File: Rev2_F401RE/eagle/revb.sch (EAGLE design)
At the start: 162 parts, among them IC1 STM32F401RE, IC2 MCP73832, IC4 TPS63001, IC5 TPS63002, J1 USB4105-GF-A, J2 MEM2051-0019500A, J200 0, Q1 SI7615, T1 MMBTA06-7-F, T10 MMBTA06-7-F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

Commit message: Add barrel jack, add headers, add jumper between buck and rail, fix OLED pinout
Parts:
- added 3V3_EN, 5V_EN, 5V_OUT: (no value), pinhead:PINHD-1X2
- added CN1: (no value), adafruit:DCBARRELPTH
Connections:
- new net 3V3_BUCK: 3V3_EN.2, C208.1, C209.1, C210.1, C211.1, IC4.FB, IC4.VOUT
- new net 5V_BUCK: 5V_EN.2, C215.1, C216.1, C217.1, C218.1, IC5.FB, IC5.VOUT
- net +3V3: now also 3V3_EN.1; no longer C208.1, C209.1, C210.1, C211.1, IC4.FB, IC4.VOUT
- net +5V: now also 5V_EN.1, 5V_OUT.1; no longer C215.1, C216.1, C217.1, C218.1, IC5.FB, IC5.VOUT
- net GND: now also 5V_OUT.2, CN1.GND
- net USB_VIN: now also CN1.PWR
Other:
- note added: "Same footprint as 47352-1001"
- moved on the sheet: 3V3, 5V, D1, D100, J1, MIDI, R100, R101, R102, R103, R104, R105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

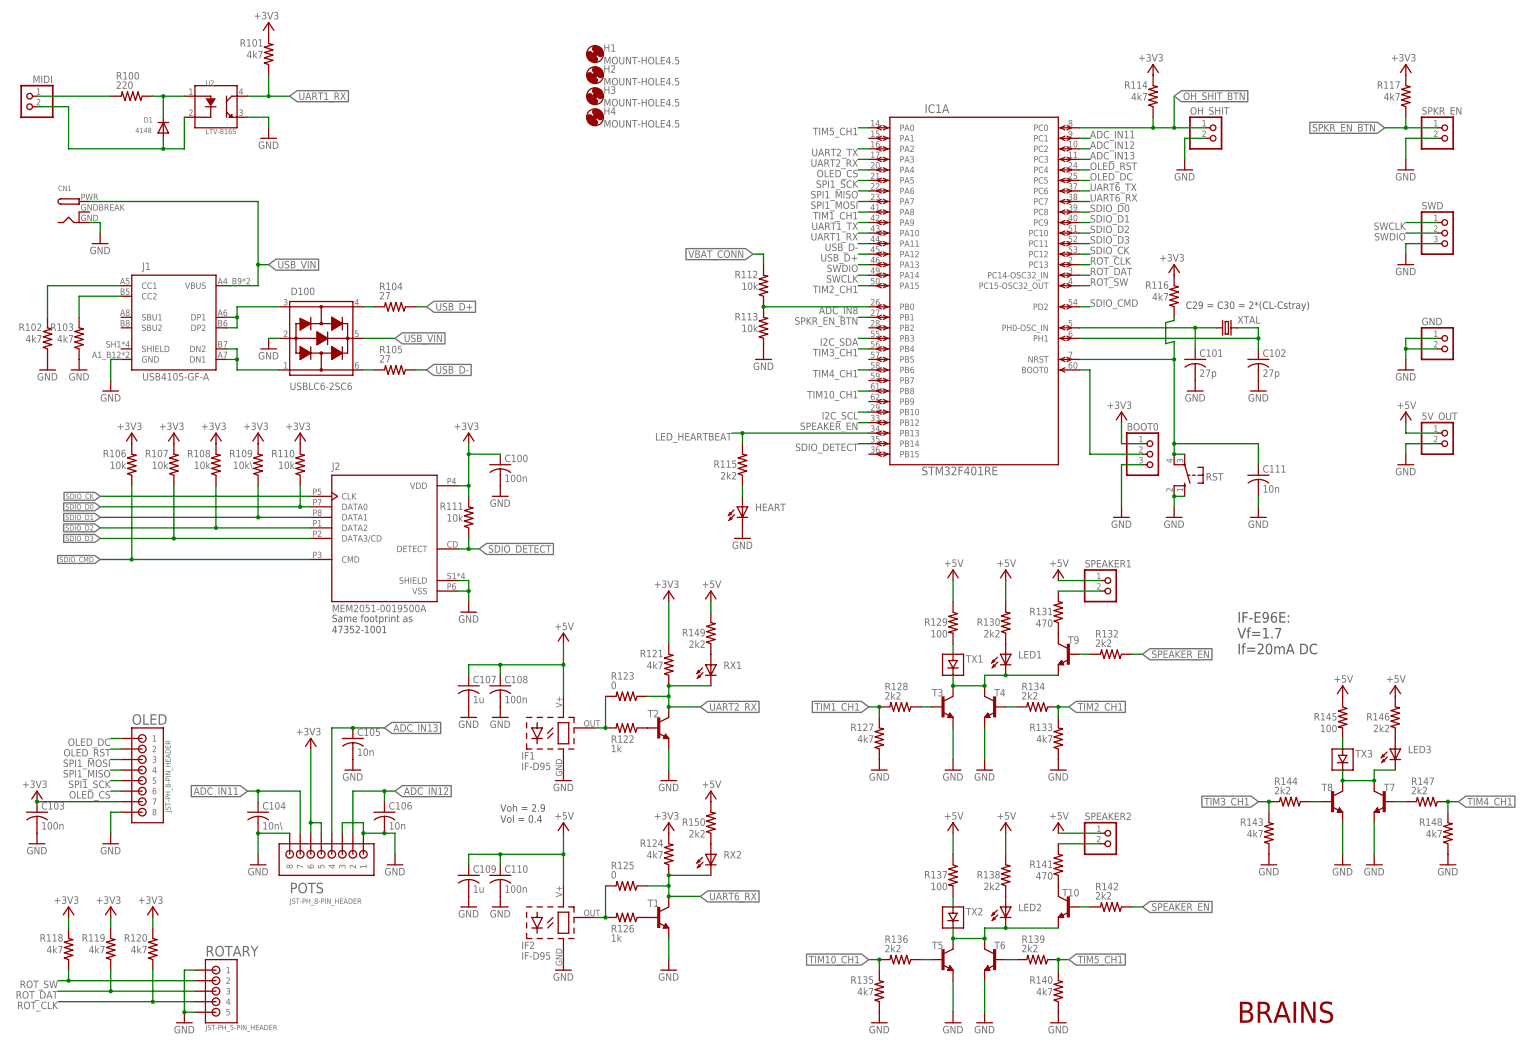
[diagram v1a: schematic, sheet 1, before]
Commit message: Add IO for a relay board
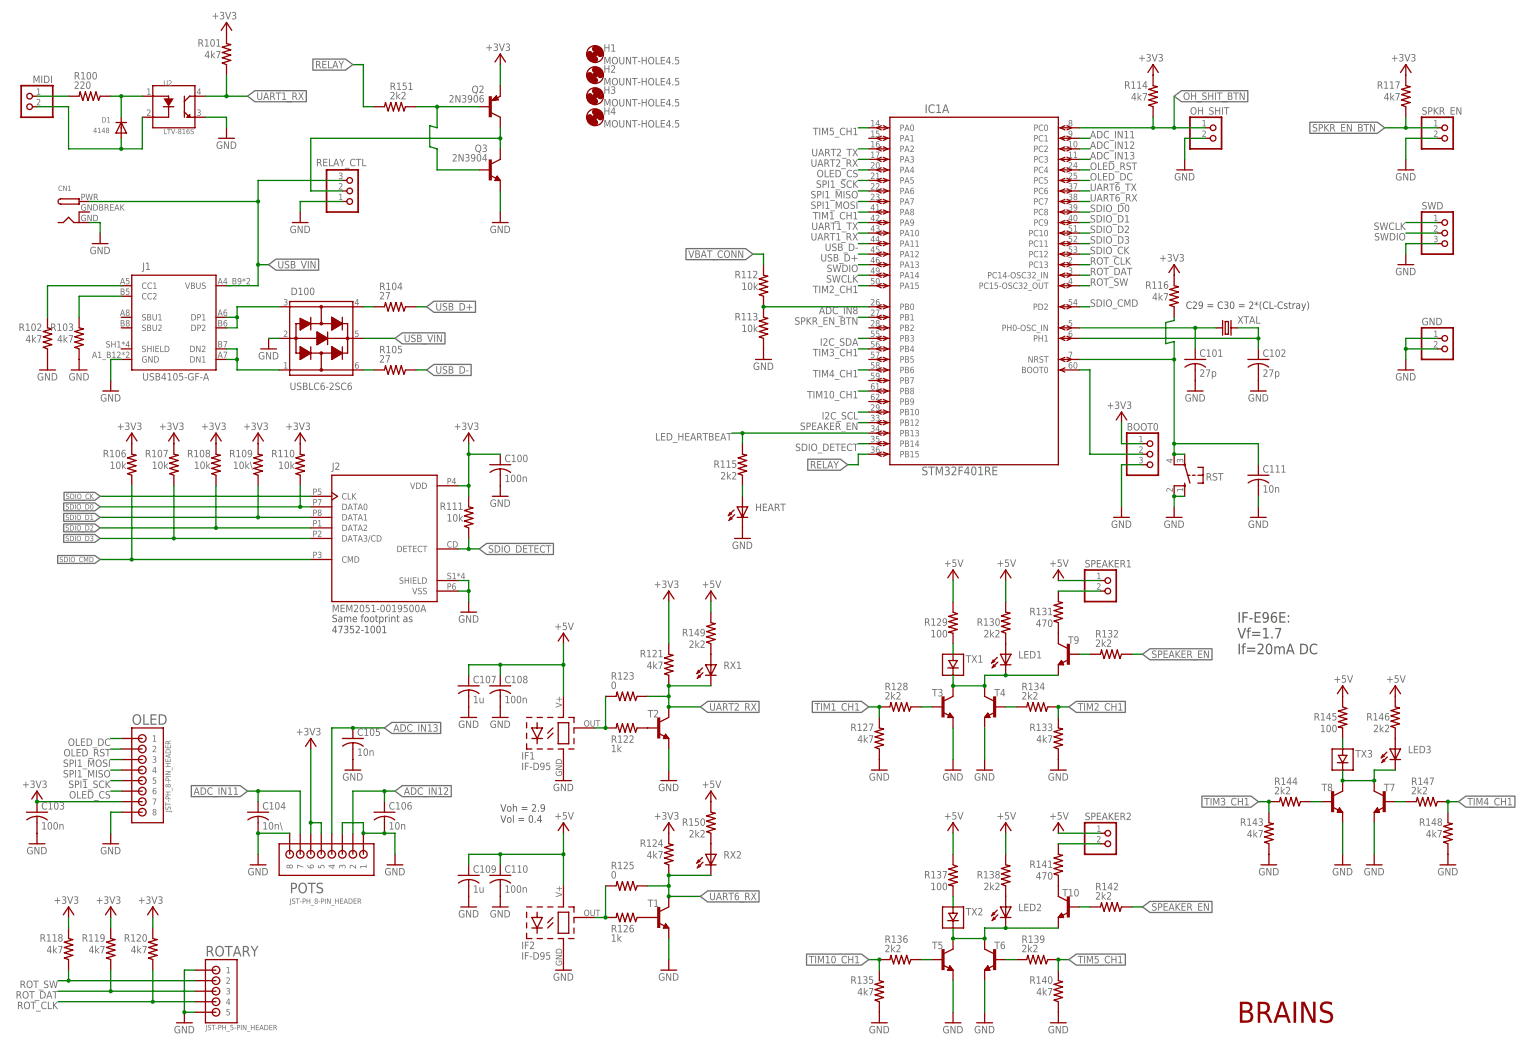
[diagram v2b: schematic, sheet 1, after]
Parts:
- removed 5V_OUT: (no value), pinhead:PINHD-1X2
- added Q2: 2N3906, transistor-pnp:2N3906
- added Q3: 2N3904, transistor-neu-to92:2N3904
- added R151: 2k2, rcl:R-US_R0603
- added RELAY_CTL: (no value), adafruit:PINHD-1X3
- renumbered R202\ to R202, R204\ to R204
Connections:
- new net RELAY: IC1A.PB15, R151.2
- new net RELAY_OUT: Q2.C, Q3.C, RELAY_CTL.2
- new net RLY_BASE: Q2.B, Q3.B, R151.1
- net +3V3: now also Q2.E
- net +5V: no longer 5V_OUT.1
- net GND: now also Q3.E, RELAY_CTL.1; no longer 5V_OUT.2
- net USB_VIN: now also RELAY_CTL.3
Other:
- moved on the sheet: D1, R100, R101, U2
